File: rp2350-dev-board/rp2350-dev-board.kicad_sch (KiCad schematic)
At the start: 40 parts, among them J1 USB_C_Receptacle_USB2.0_14P, J2 Conn_02x10_Odd_Even, J3 HDMI_A, SW1 BOOT SELECTOR, SW2 RST, U1 RP2350_60QFN, U2 AMS1117-3.3, U3 W25Q16JVSS, Y1 12Mhz HC49-SD

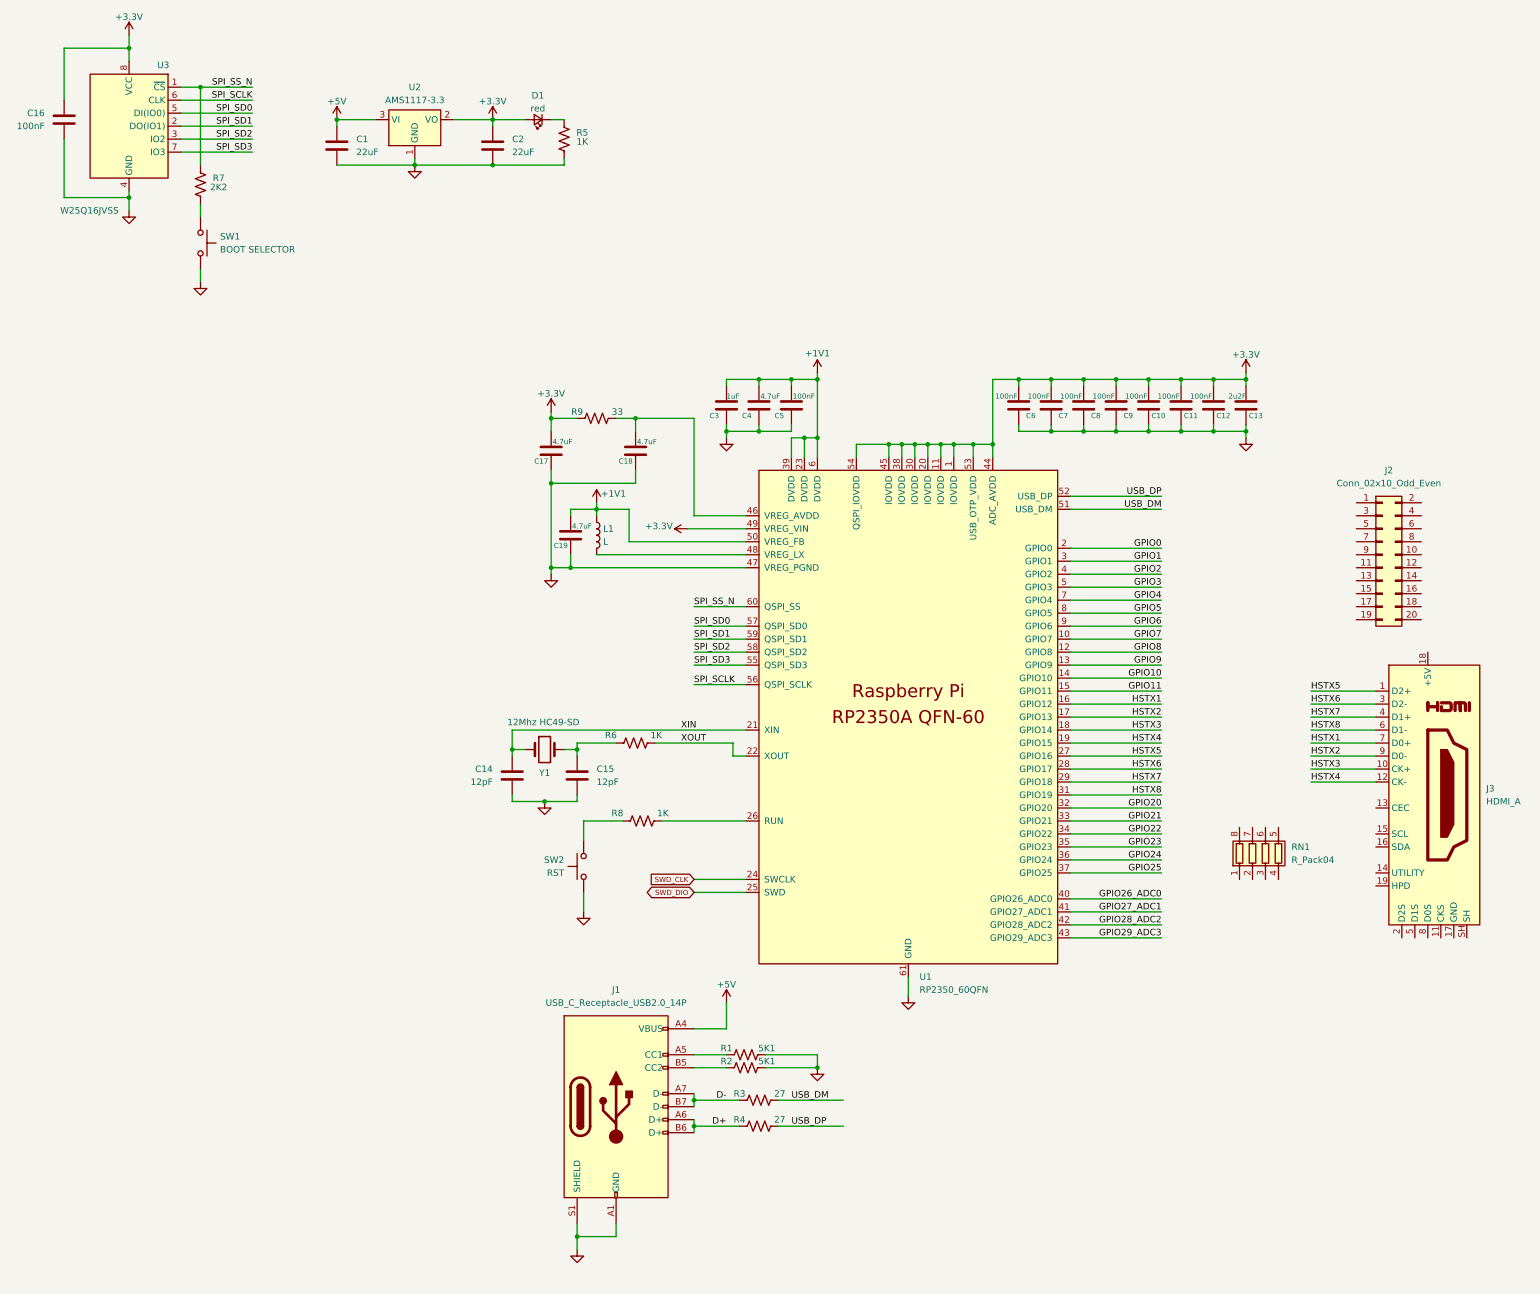
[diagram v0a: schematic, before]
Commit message: feat: finish rp2350-dev-board schematic
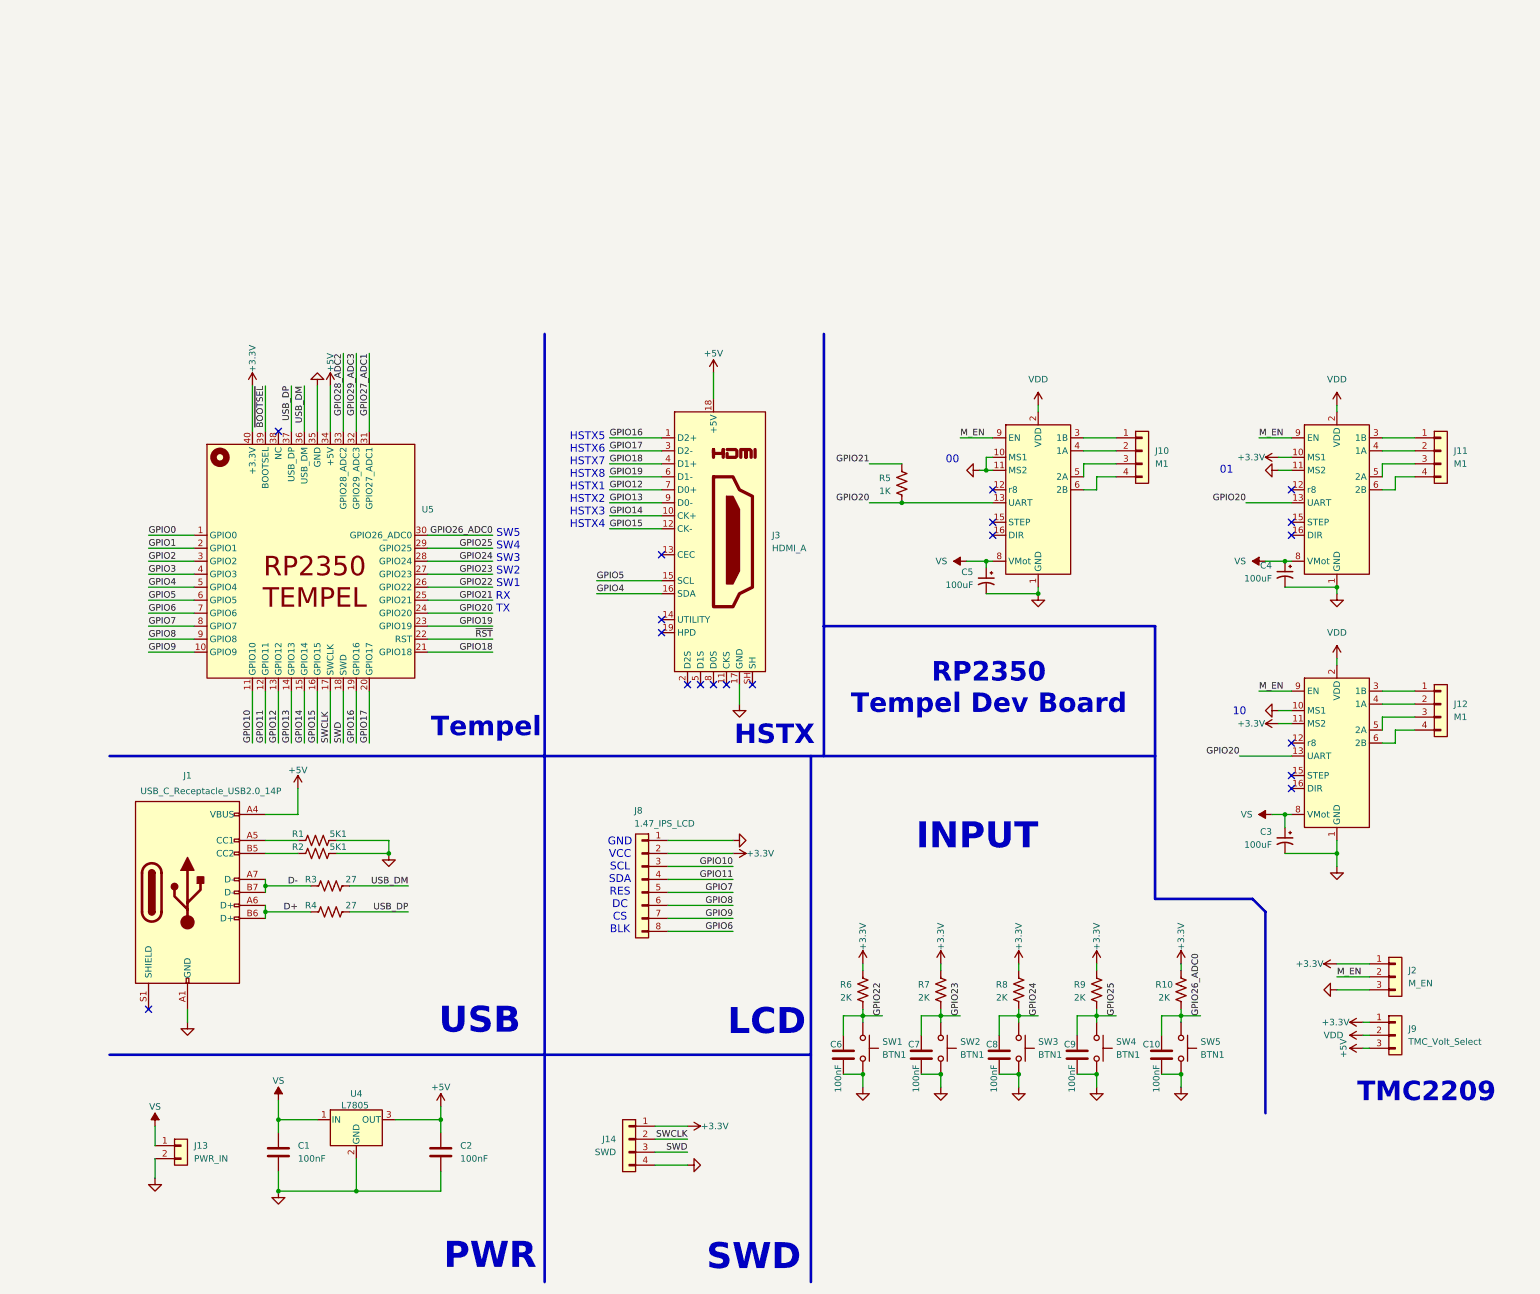
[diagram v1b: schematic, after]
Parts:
- removed C11, C12, C16, C5: 100nF, Capacitor_SMD:C_0603_1608Metric_Pad1.08x0.95mm_HandSolder, symbol Device:C
- removed C13: 2u2F, Capacitor_SMD:C_0603_1608Metric_Pad1.08x0.95mm_HandSolder, symbol Device:C
- removed C14, C15: 12pF, Capacitor_SMD:C_0603_1608Metric_Pad1.08x0.95mm_HandSolder, symbol Device:C
- removed C17, C18, C19, C4: 4.7uF, Capacitor_SMD:C_0603_1608Metric_Pad1.08x0.95mm_HandSolder, symbol Device:C
- removed C3: 1uF, Capacitor_SMD:C_0603_1608Metric_Pad1.08x0.95mm_HandSolder, symbol Device:C
- removed D1: red, LED_SMD:LED_0805_2012Metric_Pad1.15x1.40mm_HandSolder, symbol Device:LED_Small
- removed J2: Conn_02x10_Odd_Even, Connector_IDC:IDC-Header_2x10_P2.54mm_Horizontal, symbol Connector_Generic:Conn_02x10_Odd_Even
- removed L1: L, Inductor_SMD:L_0805_2012Metric_Pad1.15x1.40mm_HandSolder, symbol Device:L
- removed RN1: R_Pack04, Resistor_SMD:R_Array_Convex_4x0603, symbol Device:R_Pack04
- removed U1: RP2350_60QFN, lib:RP2350-QFN-60-1EP_7x7_P0.4mm_EP3.4x3.4mm_ThermalVias, symbol MCU_RaspberryPi_RP2350:RP2350_60QFN
- removed U2: AMS1117-3.3, Package_TO_SOT_SMD:SOT-223-3_TabPin2, symbol Regulator_Linear:AMS1117-3.3
- removed U3: W25Q16JVSS, Package_SO:SOIC-8_5.23x5.23mm_P1.27mm, symbol Memory_Flash:W25Q32JVSS
- removed Y1: 12Mhz HC49-SD, Crystal:Crystal_SMD_HC49-SD, symbol Device:Crystal
- added C3, C4, C5: 100uF, Capacitor_THT:CP_Radial_D6.3mm_P2.50mm, symbol Device:C_Polarized_Small_US
- added J10, J11, J12: M1, Connector_Hirose:Hirose_DF13-04P-1.25DSA_1x04_P1.25mm_Vertical, symbol Connector_Generic:Conn_01x04
- added J13: PWR_IN, Connector_Hirose:Hirose_DF13-02P-1.25DSA_1x02_P1.25mm_Vertical, symbol Connector_Generic:Conn_01x02
- added J14: SWD, Connector_Hirose:Hirose_DF13-04P-1.25DSA_1x04_P1.25mm_Vertical, symbol Connector_Generic:Conn_01x04
- added J2: M_EN, Connector_Hirose:Hirose_DF13-03P-1.25DSA_1x03_P1.25mm_Vertical, symbol Connector_Generic:Conn_01x03
- added J8: 1.47_IPS_LCD, Connector_PinHeader_2.54mm:PinHeader_1x08_P2.54mm_Vertical, symbol Connector_Generic:Conn_01x08
- added J9: TMC_Volt_Select, Connector_Hirose:Hirose_DF13-03P-1.25DSA_1x03_P1.25mm_Vertical, symbol Connector_Generic:Conn_01x03
- added R10: 2K, Resistor_SMD:R_0805_2012Metric_Pad1.20x1.40mm_HandSolder, symbol Device:R_US
- added SW3, SW4, SW5: BTN1, Button_Switch_SMD:SW_Push_1P1T_NO_6x6mm_H9.5mm, symbol Switch:SW_Push
- added U1, U2, U3: ~, rp2350-tempel-lib:TMC2209_MKS_V2, symbol rp2350-tempel-lib:TMC2209_MKS_V2
- added U4: L7805, Package_TO_SOT_THT:TO-220-3_Horizontal_TabDown, symbol Regulator_Linear:L7805
- added U5: ~, rp2350-tempel-lib:RP2350_Tempel_Footprint, symbol rp2350-tempel-lib:rp2350_tempel
- C1, C2: value 22uF -> 100nF; footprint Capacitor_SMD:C_0603_1608Metric_Pad1.08x0.95mm_HandSolder -> Capacitor_SMD:C_0805_2012Metric_Pad1.18x1.45mm_HandSolder
- C10, C6, C7, C8, C9: footprint Capacitor_SMD:C_0603_1608Metric_Pad1.08x0.95mm_HandSolder -> Capacitor_SMD:C_0805_2012Metric_Pad1.18x1.45mm_HandSolder
- R6, R8: value 1K -> 2K
- R7: value 2K2 -> 2K
- R9: value 33 -> 2K
- SW1: value BOOT SELECTOR -> BTN1
- SW2: value RST -> BTN1
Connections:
- net SPI_SS_N is gone; now on net GPIO23: R7.1
- net XOUT is gone; now on net +3.3V: R6.2
- net +3.3V: now also R7.2, R8.2, R9.2, J14.1 (Pin_1), J2.1 (Pin_1), J8.2 (Pin_2), J9.1 (Pin_1), R10.2, U2.10 (MS1), U3.11 (MS2), U5.40 (+3.3V); no longer C10.1, C2.1, C6.1, C7.1, C8.1, C9.1, R9.1
- net +5V: now also C2.1, J3.18 (+5V), J9.3 (Pin_3), U4.3 (OUT), U5.34 (+5V); no longer C1.1
- net GND: now also J3.17 (GND), C3.2, C4.2, C5.2, J13.2 (Pin_2), J14.4 (Pin_4), J2.3 (Pin_3), J8.1 (Pin_1), SW3.2, SW4.2, SW5.2, U1.1 (GND), U1.10 (MS1), U1.11 (MS2), U2.1 (GND), U2.11 (MS2), U3.1 (GND), U3.10 (MS1), U4.2 (GND), U5.35 (GND); no longer J1.S1 (SHIELD), R5.2
- net GPIO0: now also U5.1 (GPIO0)
- net GPIO1: now also U5.2 (GPIO1)
- net GPIO10: now also J8.3 (Pin_3), U5.11 (GPIO10)
- net GPIO11: now also J8.4 (Pin_4), U5.12 (GPIO11)
- net GPIO2: now also U5.3 (GPIO2)
- net GPIO20: now also R5.1, U1.13 (UART), U2.13 (UART), U3.13 (UART), U5.24 (GPIO20)
- net GPIO21: now also R5.2, U5.25 (GPIO21)
- net GPIO22: now also C6.1, R6.1, SW1.1, U5.26 (GPIO22)
- net GPIO23: now also C7.1, SW2.1, U5.27 (GPIO23)
- net GPIO24: now also C8.1, R8.1, SW3.1, U5.28 (GPIO24)
- net GPIO25: now also C9.1, R9.1, SW4.1, U5.29 (GPIO25)
- net GPIO26_ADC0: now also C10.1, R10.1, SW5.1, U5.30 (GPIO26_ADC0)
- net GPIO27_ADC1: now also U5.31 (GPIO27_ADC1)
- net GPIO28_ADC2: now also U5.33 (GPIO28_ADC2)
- net GPIO29_ADC3: now also U5.32 (GPIO29_ADC3)
- net GPIO3: now also U5.4 (GPIO3)
- net GPIO4: now also J3.16 (SDA), U5.5 (GPIO4)
- net GPIO5: now also J3.15 (SCL), U5.6 (GPIO5)
- net GPIO6: now also J8.8 (Pin_8), U5.7 (GPIO6)
- net GPIO7: now also J8.5 (Pin_5), U5.8 (GPIO7)
- net GPIO8: now also J8.6 (Pin_6), U5.9 (GPIO8)
- net GPIO9: now also J8.7 (Pin_7), U5.10 (GPIO9)
- net USB_DM: now also U5.36 (USB_DM)
- net USB_DP: now also U5.37 (USB_DP)
- net HSTX1 renamed GPIO12
- net GPIO12: now also U5.13 (GPIO12)
- net HSTX2 renamed GPIO13
- net GPIO13: now also U5.14 (GPIO13)
- net HSTX3 renamed GPIO14
- net GPIO14: now also U5.15 (GPIO14)
- net HSTX4 renamed GPIO15
- net GPIO15: now also U5.16 (GPIO15)
- net HSTX5 renamed GPIO16
- net GPIO16: now also U5.19 (GPIO16)
- net HSTX6 renamed GPIO17
- net GPIO17: now also U5.20 (GPIO17)
- net HSTX7 renamed GPIO18
- net GPIO18: now also U5.21 (GPIO18)
- net HSTX8 renamed GPIO19
- net GPIO19: now also U5.23 (GPIO19)
- new net: J10.1 (Pin_1), U1.3 (1B)
- new net: J10.2 (Pin_2), U1.4 (1A)
- new net: J10.3 (Pin_3), U1.5 (2A)
- new net: J10.4 (Pin_4), U1.6 (2B)
- new net: J12.1 (Pin_1), U3.3 (1B)
- new net: J12.2 (Pin_2), U3.4 (1A)
- new net: J12.3 (Pin_3), U3.5 (2A)
- new net: J12.4 (Pin_4), U3.6 (2B)
- new net: J11.1 (Pin_1), U2.3 (1B)
- new net: J11.2 (Pin_2), U2.4 (1A)
- new net: J11.3 (Pin_3), U2.5 (2A)
- new net: J11.4 (Pin_4), U2.6 (2B)
- new net M_EN: J2.2 (Pin_2), U1.9 (EN), U2.9 (EN), U3.9 (EN)
- new net SWCLK: J14.2 (Pin_2), U5.17 (SWCLK)
- new net SWD: J14.3 (Pin_3), U5.18 (SWD)
- new net VDD: J9.2 (Pin_2), U1.2 (VDD), U2.2 (VDD), U3.2 (VDD)
- new net VS: C1.1, C3.1, C4.1, C5.1, J13.1 (Pin_1), U1.8 (VMot), U2.8 (VMot), U3.8 (VMot), U4.1 (IN)
- new net ~{BOOTSEL}: U5.39 (BOOTSEL)
- new net ~{RST}: U5.22 (RST)
- no-connect marks 0 -> 19
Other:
- note added: "00"
- note added: "01"
- note added: "10"
- note added: "GND VCC SCL SDA RES DC CS BLK"
- note added: "HSTX"
- note added: "HSTX5 HSTX6 HSTX7 HSTX8 HSTX1 HSTX2 HSTX3 HSTX4"
- note added: "INPUT"
- note added: "LCD"
- note added: "PWR"
- note added: "RP2350 Tempel Dev Board"
- note added: "RX TX"
- note added: "SW5 SW4 SW3 SW2 SW1"
- note added: "SWD"
- note added: "TMC2209"
- note added: "Tempel"
- note added: "USB"
- title: (none) -> RP2350 Dev Board V001
- moved on the sheet: J3

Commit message: feat: add crumbs-rp2350 to test hstx
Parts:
- U1, U2, U3, U5: value ~ -> (none)

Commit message: feat(rp2350-devboard): copying tmc2209 and rp2350a-tempel into rp2350a devboard
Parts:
- removed C3, C4, C5: 100uF, Capacitor_THT:CP_Radial_D6.3mm_P2.50mm, symbol Device:C_Polarized_Small_US
- removed J10, J11, J12: M1, Connector_Hirose:Hirose_DF13-04P-1.25DSA_1x04_P1.25mm_Vertical, symbol Connector_Generic:Conn_01x04
- removed J2: M_EN, Connector_Hirose:Hirose_DF13-03P-1.25DSA_1x03_P1.25mm_Vertical, symbol Connector_Generic:Conn_01x03
- removed J9: TMC_Volt_Select, Connector_Hirose:Hirose_DF13-03P-1.25DSA_1x03_P1.25mm_Vertical, symbol Connector_Generic:Conn_01x03
- removed R5: 1K, Resistor_SMD:R_0805_2012Metric_Pad1.20x1.40mm_HandSolder, symbol Device:R_US
- removed U1, U2, U3: (no value), rp2350-tempel-lib:TMC2209_MKS_V2, symbol rp2350-tempel-lib:TMC2209_MKS_V2
- removed U5: (no value), rp2350-tempel-lib:RP2350_Tempel_Footprint, symbol rp2350-tempel-lib:rp2350_tempel
- added C11, C12, C13, C14: 100nF, Capacitor_SMD:C_0805_2012Metric_Pad1.18x1.45mm_HandSolder, symbol Device:C
- added C15: 22nF/50V, Capacitor_SMD:C_0805_2012Metric_Pad1.18x1.45mm_HandSolder, symbol Device:C
- added C16, C17: 4.7uF, Capacitor_SMD:C_0805_2012Metric_Pad1.18x1.45mm_HandSolder, symbol Device:C
- added C18: 100uF, Capacitor_THT:CP_Radial_D8.0mm_P3.50mm, symbol Device:C_Polarized
- added C19: 2.2uF to 4.7uF/50V, Capacitor_SMD:C_0805_2012Metric_Pad1.18x1.45mm_HandSolder, symbol Device:C
- added C20, C22: 22uF, Capacitor_SMD:C_0603_1608Metric_Pad1.08x0.95mm_HandSolder, symbol Device:C
- added C21, C30, C31, C32, C33, C34, C35, C36, C37: 100nF, Capacitor_SMD:C_0603_1608Metric_Pad1.08x0.95mm_HandSolder, symbol Device:C
- added C23, C26: 12pF, Capacitor_SMD:C_0603_1608Metric_Pad1.08x0.95mm_HandSolder, symbol Device:C
- added C24, C25, C27, C29: 4.7uF, Capacitor_SMD:C_0603_1608Metric_Pad1.08x0.95mm_HandSolder, symbol Device:C
- added C28: 1uF, Capacitor_SMD:C_0603_1608Metric_Pad1.08x0.95mm_HandSolder, symbol Device:C
- added C38: 2u2F, Capacitor_SMD:C_0603_1608Metric_Pad1.08x0.95mm_HandSolder, symbol Device:C
- added D1: DIAG, LED_SMD:LED_0805_2012Metric_Pad1.15x1.40mm_HandSolder, symbol Device:LED
- added D2: red, LED_SMD:LED_0805_2012Metric_Pad1.15x1.40mm_HandSolder, symbol Device:LED_Small
- added J15: TMC2209_VIN, TerminalBlock_Phoenix:TerminalBlock_Phoenix_PT-1,5-2-5.0-H_1x02_P5.00mm_Horizontal, symbol Connector:Screw_Terminal_01x02
- added J16: TMC2209_Conn, Connector_Molex:Molex_Nano-Fit_105313-xx04_1x04_P2.50mm_Horizontal, symbol Connector_Generic:Conn_01x04
- added J17: Conn_West, Connector_PinHeader_2.54mm:PinHeader_1x10_P2.54mm_Vertical, symbol Connector_Generic:Conn_01x10
- added J18: Conn_North, Connector_PinHeader_2.54mm:PinHeader_1x10_P2.54mm_Vertical, symbol Connector_Generic:Conn_01x10
- added J19: Conn_South, Connector_PinHeader_2.54mm:PinHeader_1x10_P2.54mm_Vertical, symbol Connector_Generic:Conn_01x10
- added J20: Conn_East, Connector_PinHeader_2.54mm:PinHeader_1x10_P2.54mm_Vertical, symbol Connector_Generic:Conn_01x10
- added J4: MS1, Connector_PinHeader_2.54mm:PinHeader_1x03_P2.54mm_Vertical, symbol Connector_Generic:Conn_01x03
- added J5: MS2, Connector_PinHeader_2.54mm:PinHeader_1x03_P2.54mm_Vertical, symbol Connector_Generic:Conn_01x03
- added J6: Spread, Connector_PinHeader_2.54mm:PinHeader_1x03_P2.54mm_Vertical, symbol Connector_Generic:Conn_01x03
- added J7: DriverConn, Connector_IDC:IDC-Header_2x05_P2.54mm_Vertical, symbol Connector_Generic:Conn_02x05_Odd_Even
- added JP1: BRA, Jumper:SolderJumper-2_P1.3mm_Open_RoundedPad1.0x1.5mm, symbol Jumper:SolderJumper_2_Open
- added JP2: BRB, Jumper:SolderJumper-2_P1.3mm_Open_RoundedPad1.0x1.5mm, symbol Jumper:SolderJumper_2_Open
- added L1: 3.3uH, Inductor_SMD:L_0805_2012Metric_Pad1.05x1.20mm_HandSolder, symbol Device:L
- added R11: 20K, Resistor_SMD:R_0805_2012Metric_Pad1.20x1.40mm_HandSolder, symbol Device:R_US
- added R12, R14: 100K, Resistor_SMD:R_0805_2012Metric_Pad1.20x1.40mm_HandSolder, symbol Device:R_US
- added R13: 220, Resistor_SMD:R_0805_2012Metric_Pad1.20x1.40mm_HandSolder, symbol Device:R_US
- added R15, R16: 120m 1W 2010, Resistor_SMD:R_2010_5025Metric, symbol Device:R_US
- added R17: 10K, Resistor_SMD:R_0805_2012Metric_Pad1.20x1.40mm_HandSolder, symbol Device:R_US
- added R18: 2K2, Resistor_SMD:R_0805_2012Metric_Pad1.20x1.40mm_HandSolder, symbol Device:R_US
- added R19, R21, R22, R23: 1K, Resistor_SMD:R_0805_2012Metric_Pad1.20x1.40mm_HandSolder, symbol Device:R_US
- added R20: 33, Resistor_SMD:R_0805_2012Metric_Pad1.20x1.40mm_HandSolder, symbol Device:R_US
- added RV1: 10K, Potentiometer_SMD:Potentiometer_Bourns_3269W_Vertical, symbol Device:R_Potentiometer_US
- added SW6: BOOT SELECTOR, Button_Switch_SMD:SW_Push_1P1T_NO_CK_KMR2, symbol Switch:SW_Push
- added SW7: RST, Button_Switch_SMD:SW_Push_1P1T_NO_CK_KMR2, symbol Switch:SW_Push
- added U6: TMC2209-LA, Package_DFN_QFN:VQFN-28-1EP_5x5mm_P0.5mm_EP3.7x3.7mm, symbol Driver_Motor:TMC2209-LA
- added U7: W25Q16JVSS, Package_SO:SOIC-8_5.3x5.3mm_P1.27mm, symbol Memory_Flash:W25Q32JVSS
- added U8: AMS1117-3.3, Package_TO_SOT_SMD:SOT-223-3_TabPin2, symbol Regulator_Linear:AMS1117-3.3
- added U9: RP2350_60QFN, lib:RP2350-QFN-60-1EP_7x7_P0.4mm_EP3.4x3.4mm_ThermalVias, symbol MCU_RaspberryPi_RP2350:RP2350_60QFN
- added Y1: 12Mhz HC49-SD, Crystal:Crystal_SMD_HC49-SD, symbol Device:Crystal
- J14: footprint Connector_Hirose:Hirose_DF13-04P-1.25DSA_1x04_P1.25mm_Vertical -> Connector_Molex:Molex_Micro-Latch_53253-0470_1x04_P2.00mm_Vertical
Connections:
- net +3.3V: now also C11.1, C21.1, C22.1, C24.1, C31.1, C32.1, C33.1, C34.1, C35.1, C36.1, C37.1, C38.1, D2.2 (A), J18.1 (Pin_1), J4.1 (Pin_1), J5.1 (Pin_1), J6.1 (Pin_1), J7.4 (Pin_4), R20.1, R21.2, U6.15 (VCC_IO), U7.8 (VCC), U8.2 (VO), U9.1 (IOVDD), U9.11 (IOVDD), U9.20 (IOVDD), U9.26 (RUN), U9.30 (IOVDD), U9.38 (IOVDD), U9.44 (ADC_AVDD), U9.45 (IOVDD), U9.49 (VREG_VIN), U9.53 (USB_OTP_VDD), U9.54 (QSPI_IOVDD)
- net +5V: now also C20.1, J18.7 (Pin_7), J7.2 (Pin_2), R17.1, U8.3 (VI)
- net GND: now also C11.2, C13.2, C14.2, C16.2, C17.2, C18.2, C19.2, C20.2, C21.2, C22.2, C23.2, C24.2, C25.2, C26.2, C27.2, C28.2, C29.2, C30.2, C31.2, C32.2, C33.2, C34.2, C35.2, C36.2, C37.2, C38.2, D1.1 (K), J15.2 (Pin_2), J18.6 (Pin_6), J4.3 (Pin_3), J5.3 (Pin_3), J6.3 (Pin_3), J7.10 (Pin_10), JP1.1 (A), JP2.1 (A), R11.2, R12.2, R14.2, R15.2, R16.2, R19.2, RV1.3, SW6.2, SW7.2, U6.18 (GND), U6.29 (GND), U6.3 (GND), U7.4 (GND), U8.1 (GND), U9.47 (VREG_PGND), U9.61 (GND)
- net GPIO0: now also J17.1 (Pin_1), U9.2 (GPIO0)
- net GPIO1: now also J17.2 (Pin_2), U9.3 (GPIO1)
- net GPIO10: now also J19.1 (Pin_1), U9.14 (GPIO10)
- net GPIO11: now also J19.2 (Pin_2), U9.15 (GPIO11)
- net GPIO12: now also J19.3 (Pin_3), U9.16 (GPIO12)
- net GPIO13: now also J19.4 (Pin_4), U9.17 (GPIO13)
- net GPIO14: now also J19.5 (Pin_5), U9.18 (GPIO14)
- net GPIO15: now also J19.6 (Pin_6), U9.19 (GPIO15)
- net GPIO16: now also J19.9 (Pin_9), U9.27 (GPIO16)
- net GPIO17: now also J19.10 (Pin_10), U9.28 (GPIO17)
- net GPIO18: now also J20.10 (Pin_10), U9.29 (GPIO18)
- net GPIO19: now also J20.8 (Pin_8), U9.31 (GPIO19)
- net GPIO2: now also J17.3 (Pin_3), U9.4 (GPIO2)
- net GPIO20: now also J20.7 (Pin_7), U9.32 (GPIO20)
- net GPIO21: now also J20.6 (Pin_6), U9.33 (GPIO21)
- net GPIO22: now also J20.5 (Pin_5), U9.34 (GPIO22)
- net GPIO23: now also J20.4 (Pin_4), U9.35 (GPIO23)
- net GPIO24: now also J20.3 (Pin_3), U9.36 (GPIO24)
- net GPIO25: now also J20.2 (Pin_2), U9.37 (GPIO25)
- net GPIO26_ADC0: now also J20.1 (Pin_1), U9.40 (GPIO26_ADC0)
- net GPIO27_ADC1: now also J18.10 (Pin_10), U9.41 (GPIO27_ADC1)
- net GPIO28_ADC2: now also J18.8 (Pin_8), U9.42 (GPIO28_ADC2)
- net GPIO29_ADC3: now also J18.9 (Pin_9), U9.43 (GPIO29_ADC3)
- net GPIO3: now also J17.4 (Pin_4), U9.5 (GPIO3)
- net GPIO4: now also J17.5 (Pin_5), U9.7 (GPIO4)
- net GPIO5: now also J17.6 (Pin_6), U9.8 (GPIO5)
- net GPIO6: now also J17.7 (Pin_7), U9.9 (GPIO6)
- net GPIO7: now also J17.8 (Pin_8), U9.10 (GPIO7)
- net GPIO8: now also J17.9 (Pin_9), U9.12 (GPIO8)
- net GPIO9: now also J17.10 (Pin_10), U9.13 (GPIO9)
- net SWCLK: now also J19.7 (Pin_7), U9.24 (SWCLK)
- net SWD: now also J19.8 (Pin_8), U9.25 (SWD)
- net USB_DM: now also J18.5 (Pin_5), U9.51 (USB_DM)
- net USB_DP: now also J18.4 (Pin_4), U9.52 (USB_DP)
- net ~{BOOTSEL}: now also J18.2 (Pin_2), R18.2, SW6.1
- net ~{RST}: now also J20.9 (Pin_9), R21.1, SW7.1
- new net: C26.1, R22.1, Y1.2
- new net: J16.1 (Pin_1), U6.24 (OA1)
- new net: J16.2 (Pin_2), U6.21 (OA2)
- new net: J16.3 (Pin_3), U6.26 (OB1)
- new net: J16.4 (Pin_4), U6.1 (OB2)
- new net: D2.1 (K), R19.1
- new net: L1.2, U9.48 (VREG_LX)
- new net: JP1.2 (B), R15.1, U6.27 (BRB)
- new net: JP2.2 (B), R16.1, U6.23 (BRA)
- new net: C27.1, R20.2, U9.46 (VREG_AVDD)
- new net: R17.2, RV1.1
- new net: RV1.2, U6.17 (VREF)
- new net: C15.1, U6.4 (CPO)
- new net: C15.2, U6.5 (CPI)
- new net: R14.1, U6.13 (CLK)
- new net: D1.2 (A), R13.2
- new net: C12.2, U6.6 (VCP)
- new net +1V1: C25.1, C28.1, C29.1, C30.1, L1.1, U9.23 (DVDD), U9.39 (DVDD), U9.50 (VREG_FB), U9.6 (DVDD)
- new net +5V_INT: C19.1, U6.8 (5VOUT)
- new net DIAG: J7.7 (Pin_7), R13.1, U6.11 (DIAG)
- new net DIR: J7.3 (Pin_3), U6.19 (DIR)
- new net INDEX: J7.5 (Pin_5), U6.12 (INDEX)
- new net MS1/AD0: J4.2 (Pin_2), U6.9 (MS1/AD0)
- new net MS2/AD1: J5.2 (Pin_2), U6.10 (MS2/AD1)
- new net SPI_SCLK: U7.6 (CLK), U9.56 (QSPI_SCLK)
- new net SPI_SD0: U7.5 (DI(IO0)), U9.57 (QSPI_SD0)
- new net SPI_SD1: U7.2 (DO(IO1)), U9.59 (QSPI_SD1)
- new net SPI_SD2: U7.3 (IO2), U9.58 (QSPI_SD2)
- new net SPI_SD3: U7.7 (IO3), U9.55 (QSPI_SD3)
- new net SPI_SS_N: R18.1, U7.1 (~{CS}), U9.60 (QSPI_SS)
- new net SPREAD: J6.2 (Pin_2), U6.7 (SPREAD)
- new net STDBY: R12.1, U6.20 (STDBY)
- new net STEP: J7.1 (Pin_1), U6.16 (STEP)
- new net UART_RX: J7.6 (Pin_6), R23.1, U6.14 (~{PD}/UART)
- new net UART_TX: J7.8 (Pin_8), R23.2
- new net VM: C12.1, C13.1, C14.1, C16.1, C17.1, C18.1, J15.1 (Pin_1), U6.22 (VS), U6.28 (VS)
- new net XIN: C23.1, U9.21 (XIN), Y1.1
- new net XOUT: R22.2, U9.22 (XOUT)
- new net ~{EN}: R11.1, U6.2 (~{EN})
- no-connect marks 19 -> 12
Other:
- note added: "CLK input. Tie to GND using short wire for internal clock or supply external clock."
- note added: "Chopper mode selection: - Low=StealthChop, - High=SpreadCycle"
- note added: "Enable not input. The power stage becomes switched off (all motor outputs floating) when this pin becomes driven to a high level."
- note added: "RP2350A"
- note added: "STANDBY input. Pull up to disable driver internal supply regulator. This will bring the driver into a low power dissipation state. 100kOhm pulldown. (may be left unconnected) Hint: Also shut down VREF voltage and ENN to 0V during standby"
- note added: "all C must more than motor voltage"
- note removed: "00"
- note removed: "01"
- note removed: "10"
- note removed: "RP2350 Tempel Dev Board"
- note removed: "RX TX"
- note removed: "SW5 SW4 SW3 SW2 SW1"
- note removed: "Tempel"
- title: RP2350 Dev Board V001 -> RP2350 Dev Board V002
- moved on the sheet: C1, C10, C2, C6, C7, C8, C9, J1, J13, J14, J3, J8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
